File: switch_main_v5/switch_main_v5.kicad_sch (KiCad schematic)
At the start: 8 parts

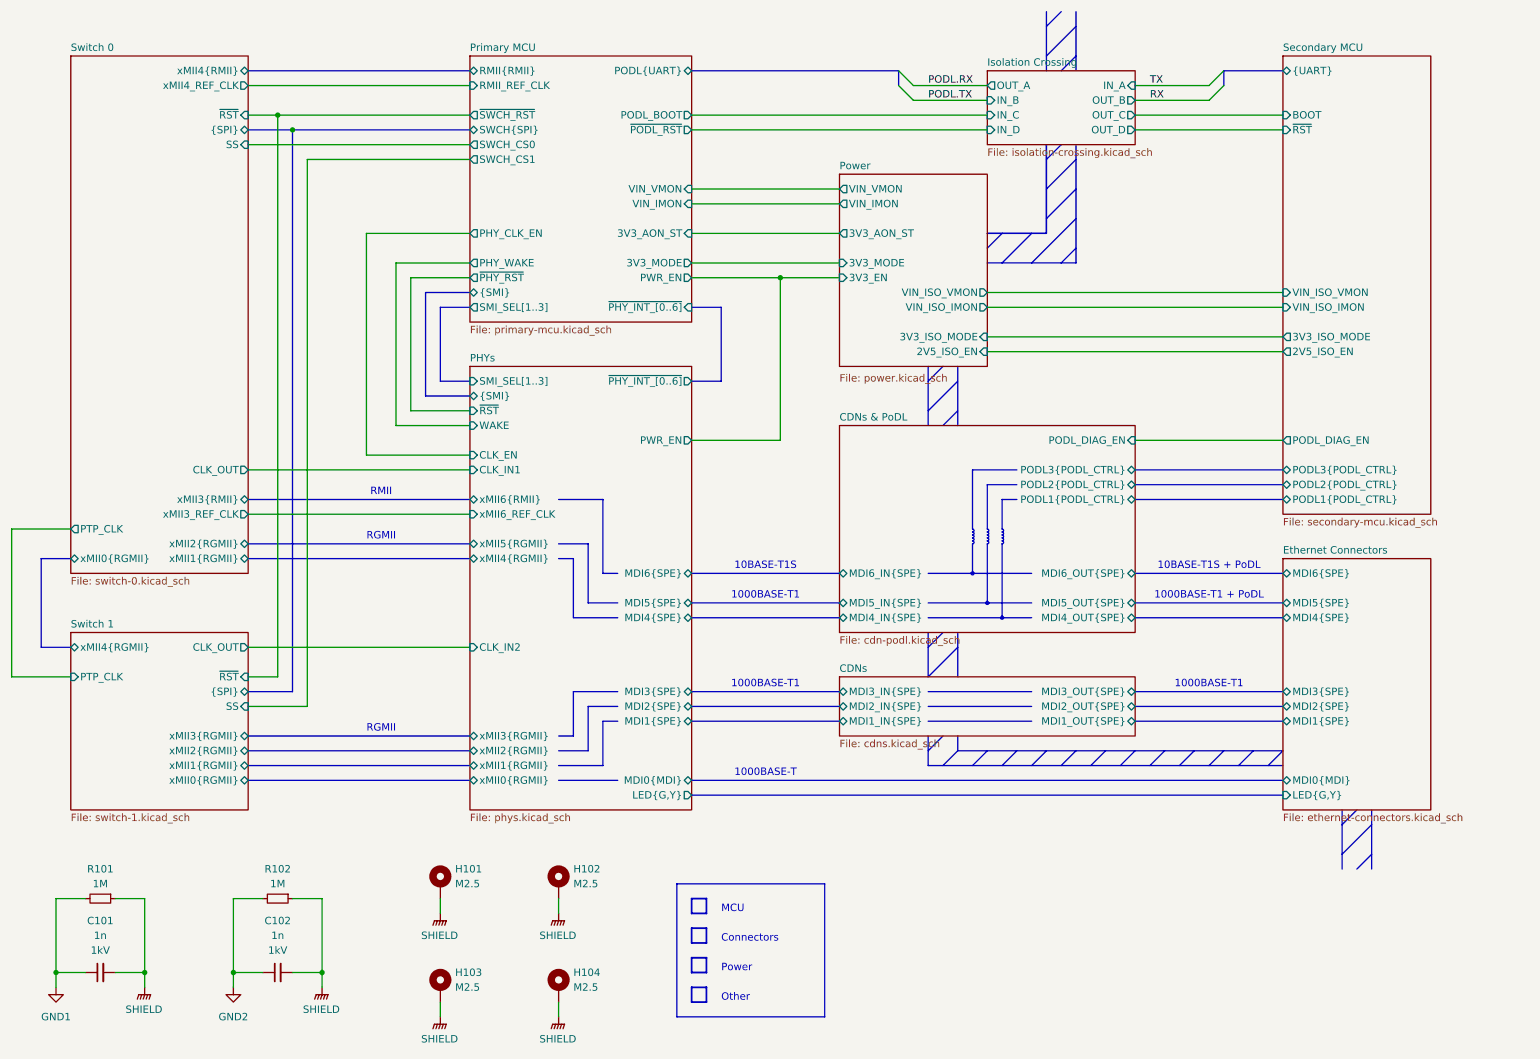
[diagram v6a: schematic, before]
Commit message: Removed one switch crystal so both are now clocked from the same source and timestamps won't drift
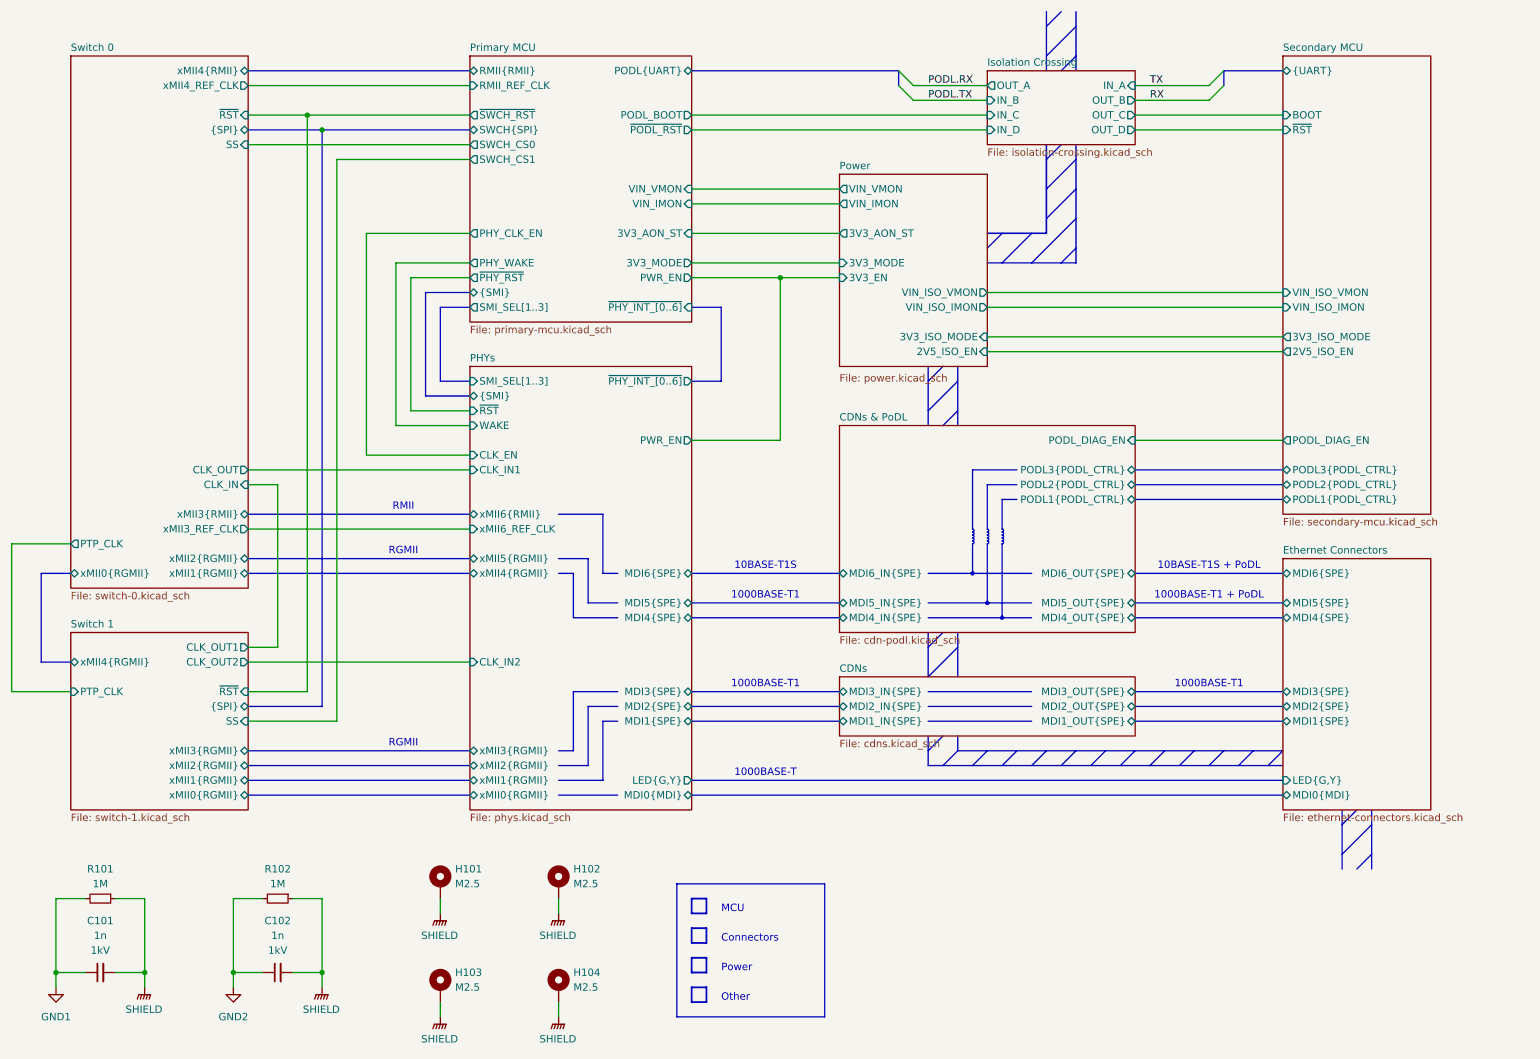
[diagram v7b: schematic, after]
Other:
- sheet Switch 0 ports: added CLK_IN; removed none
- sheet Switch 1 ports: added CLK_OUT1, CLK_OUT2; removed CLK_OUT
